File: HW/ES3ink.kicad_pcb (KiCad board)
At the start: 2 copper layers, 60.8 x 31 mm, 78 parts, among them J1 USB_C_Receptacle_USB2.0, J2 Conn_01x24_Pin, J3 Conn_01x02_Pin, J4 Conn_01x04_Socket, J5 USB_C_Receptacle_USB2.0, Q1 AO3401A, Q2 SI1308EDL-T1-GE3, Q3 DMP2045U-7, Q4 SI2305, SW1 RESET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

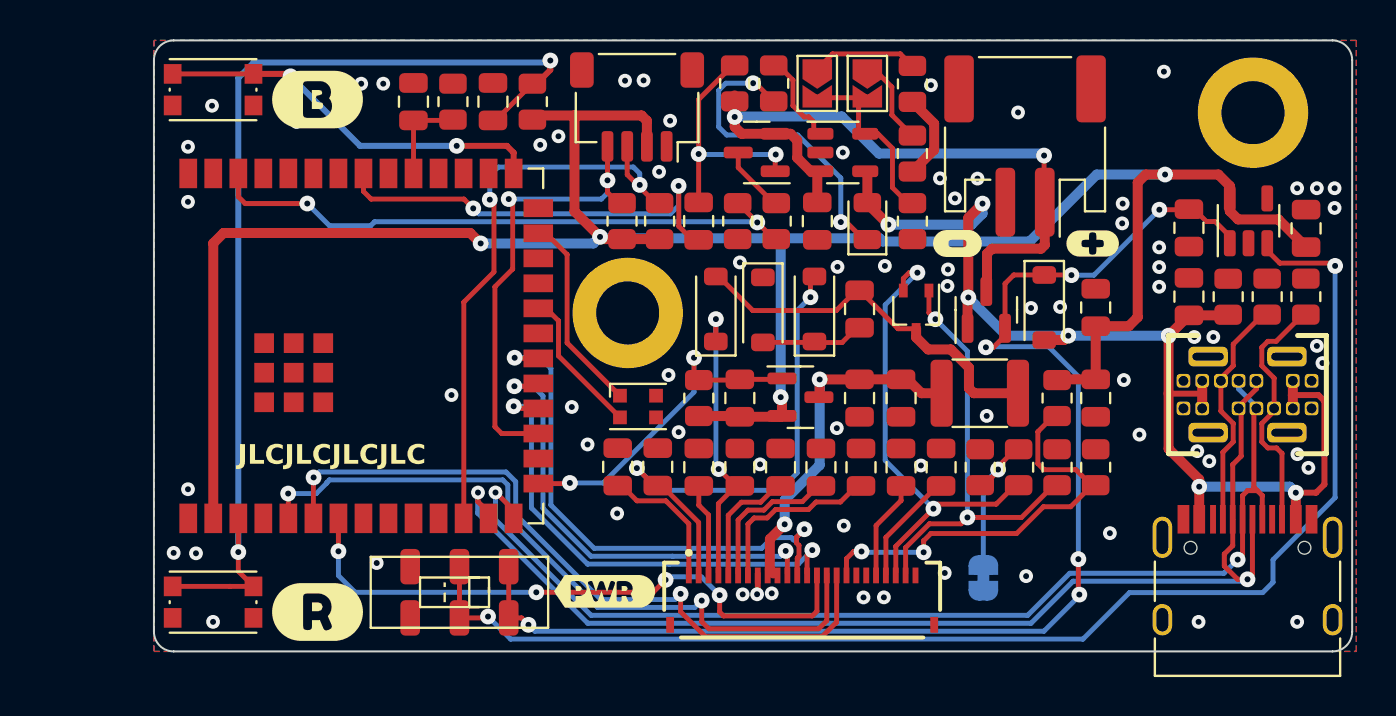
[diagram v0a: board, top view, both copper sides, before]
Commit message: Update
- changed format to KiCad 8
- changed some tracks
- add JP3 label
- add OHW logo
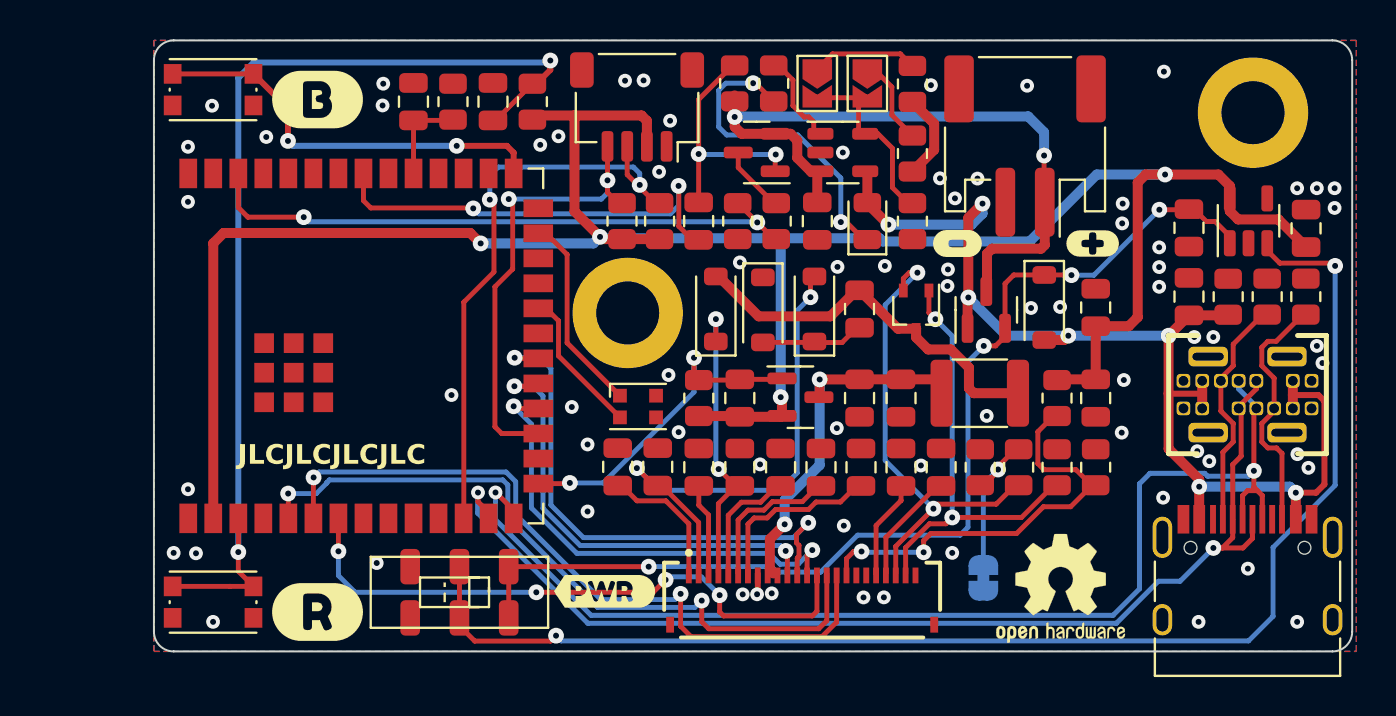
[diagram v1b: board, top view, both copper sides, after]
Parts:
- added REF**: OSHW-Logo2_7.3x6mm_SilkScreen, Symbol:OSHW-Logo2_7.3x6mm_SilkScreen, F.Cu at (155.7, 131.8)
- added kibuzzard-66550BBA: G***, kibuzzard-66550BBA, B.Cu at (154.0, 131.3)
- R18: value 1M -> 10K
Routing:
- net Net-(D5-K): track 66.8 -> 54.4 mm, vias 6 -> 4
- net /D+: track 55.8 -> 59.5 mm
- net /D-: track 59.7 -> 56.3 mm
- net Net-(SW3-B): track 67.1 -> 68.6 mm
- net /IO0: track 20.0 -> 21.0 mm
- net /BAT+: track 35.2 -> 35.9 mm

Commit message: Update
- upgrade to KiCad 9
- changed U1 from ESP32-S3-WROOM-2 to WROOM-1
- added 3D models to project
- added fiducials
- changed routing of the board
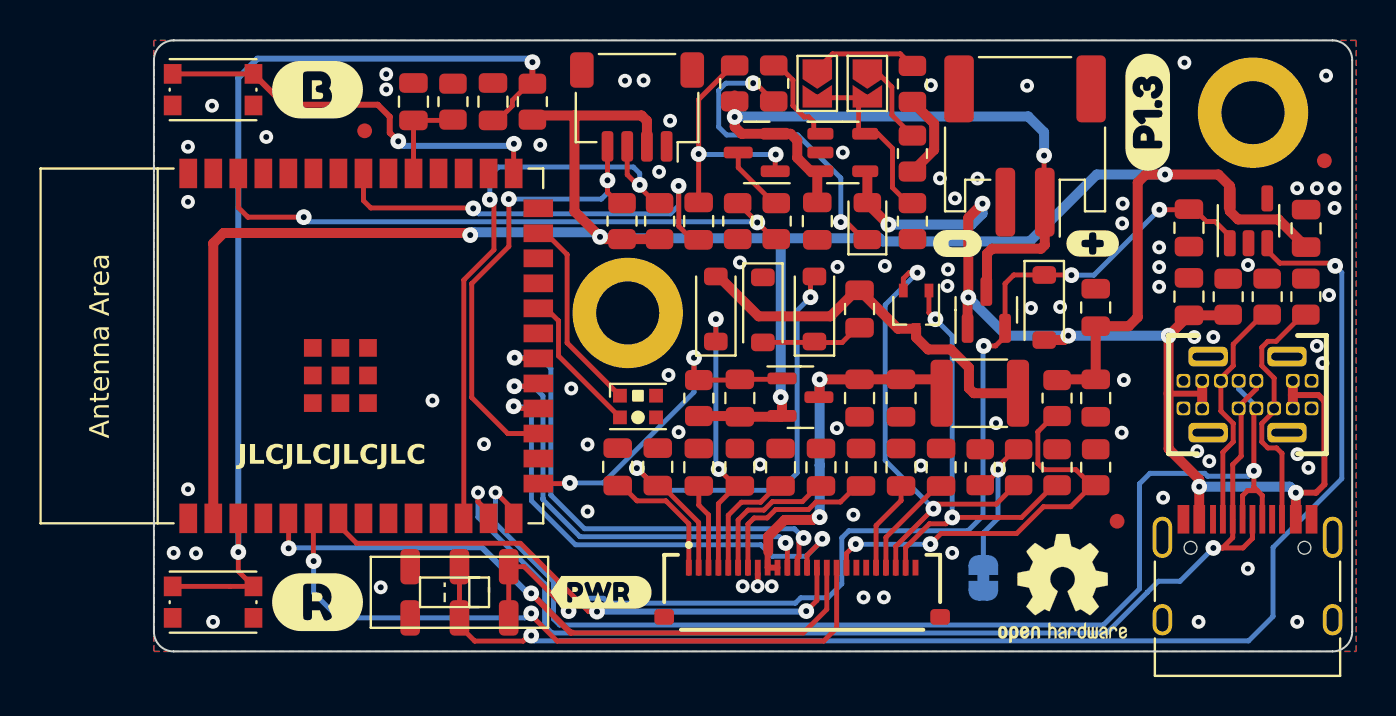
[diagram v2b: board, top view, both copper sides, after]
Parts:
- removed kibuzzard-66550BBA: G***, kibuzzard-66550BBA
- added FID1: Fiducial, Fiducial:Fiducial_0.75mm_Mask1.5mm, F.Cu at (169.1, 110.1)
- added FID2: Fiducial, Fiducial:Fiducial_0.75mm_Mask1.5mm, F.Cu at (158.6, 128.4)
- added FID3: Fiducial, Fiducial:Fiducial_0.75mm_Mask1.5mm, F.Cu at (120.4, 108.6)
- added kibuzzard-6951B36D: G***, kibuzzard-6951B36D, F.Cu at (160.1, 107.7)
- added kibuzzard-6951C433: G***, kibuzzard-6951C433, B.Cu at (140.1, 131.3)
- J3: value Conn_01x02_Pin -> BAT_CONN
- U1: value ESP32-S3-WROOM-2 -> ESP32-S3-WROOM-1; footprint ESP32_libraries:ESP32-S3-WROOM-2 -> PCM_Espressif:ESP32-S3-WROOM-1
- moved G*** 1.00 mm to (123.7, 120.0)
- moved kibuzzard-65272A96 1.00 mm to (113.7, 120.0)
- moved kibuzzard-649216A2 0.50 mm to (118.0, 132.5)
- moved kibuzzard-649216B3 0.50 mm to (118.0, 106.5)
- moved J2 0.40 mm to (142.6, 132.0)
- moved kibuzzard-659DC4DE 0.18 mm to (132.4, 132.0)
- moved REF** 0.10 mm to (155.8, 131.8)
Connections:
- net +5V renamed VBUS
- U1 pad 28: unconnected-(U1-NC-Pad28) -> /IO35
- U1 pad 29: unconnected-(U1-NC-Pad29) -> /IO36
- U1 pad 30: unconnected-(U1-NC-Pad30) -> /IO37
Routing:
- net /IO5: track 36.5 -> 32.8 mm
- net Net-(D5-K): track 54.4 -> 57.7 mm
- net /IO7: track 31.2 -> 28.3 mm, vias 4 -> 2
- net /IO6: track 37.1 -> 34.5 mm
- net /IO12: track 27.2 -> 25.4 mm
- net /D-: track 56.3 -> 58.0 mm
- net /D+: track 59.5 -> 61.2 mm
- net /IO10: track 23.9 -> 25.2 mm
- net /EN: track 52.6 -> 51.4 mm
- net /3V3_EPD: track 19.1 -> 19.7 mm
- net /IO9: track 23.4 -> 24.1 mm
- net GND: track 5.60 -> 5.18 mm, vias 71 -> 74
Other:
- board text removed: "P1.2"
